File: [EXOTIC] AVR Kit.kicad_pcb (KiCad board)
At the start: 2 copper layers, 100 x 75 mm, 58 parts, among them J1 AVR-ISP-10, J10 5 V Headers, J2 Barrel_Jack_Switch, J3 USB_B, J4 Port A, J5 Port B, J6 Port C + D7, J7 Port D, J9 3.3 V Headers, Q1 AO3401A, SW1 SW_Push, SW2 SW_DPDT_x2, U1 ATmega32A-P, U2 AMS1117-5.0, U3 AMS1117-3.3, U4 LM339, U6 CH340C, Y1 16 MHz

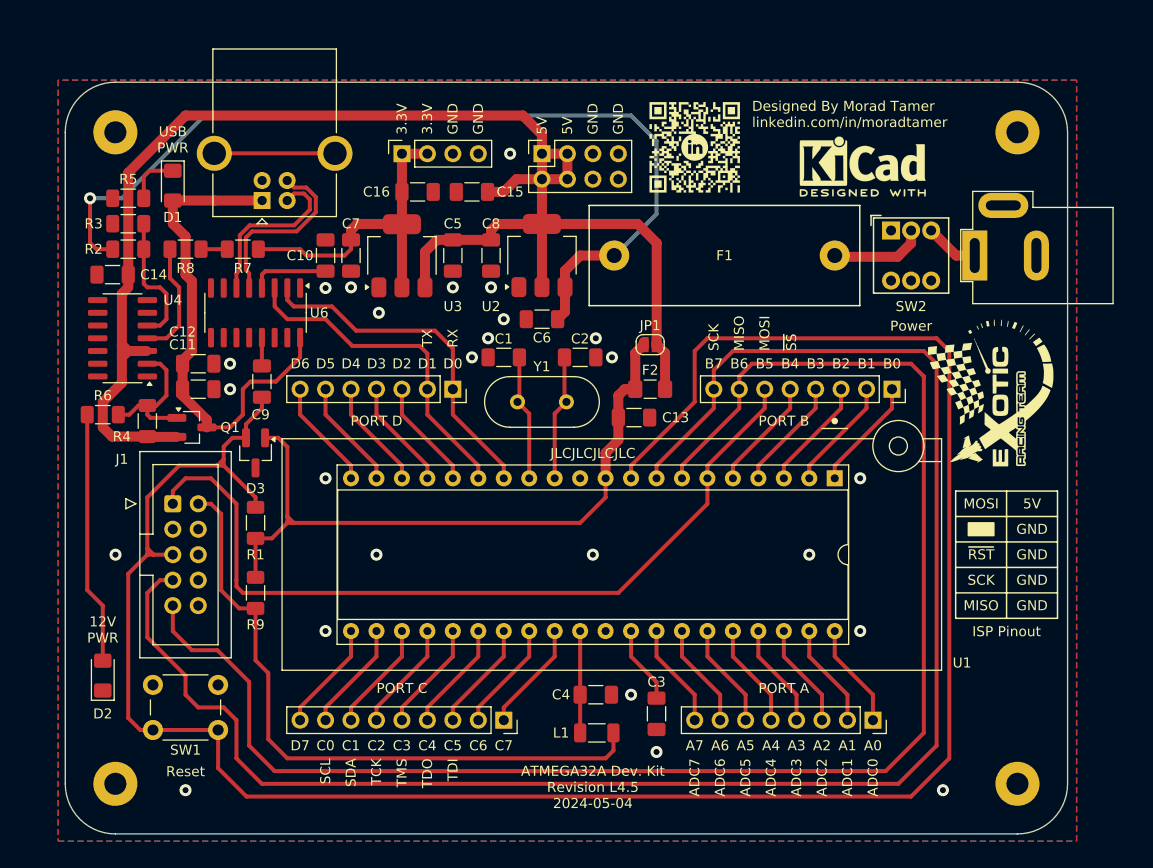
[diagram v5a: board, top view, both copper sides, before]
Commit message: Removed the two LED indicators
Removed the two LED indicators for each power source and replaced them with a single LED for the final 5V rail
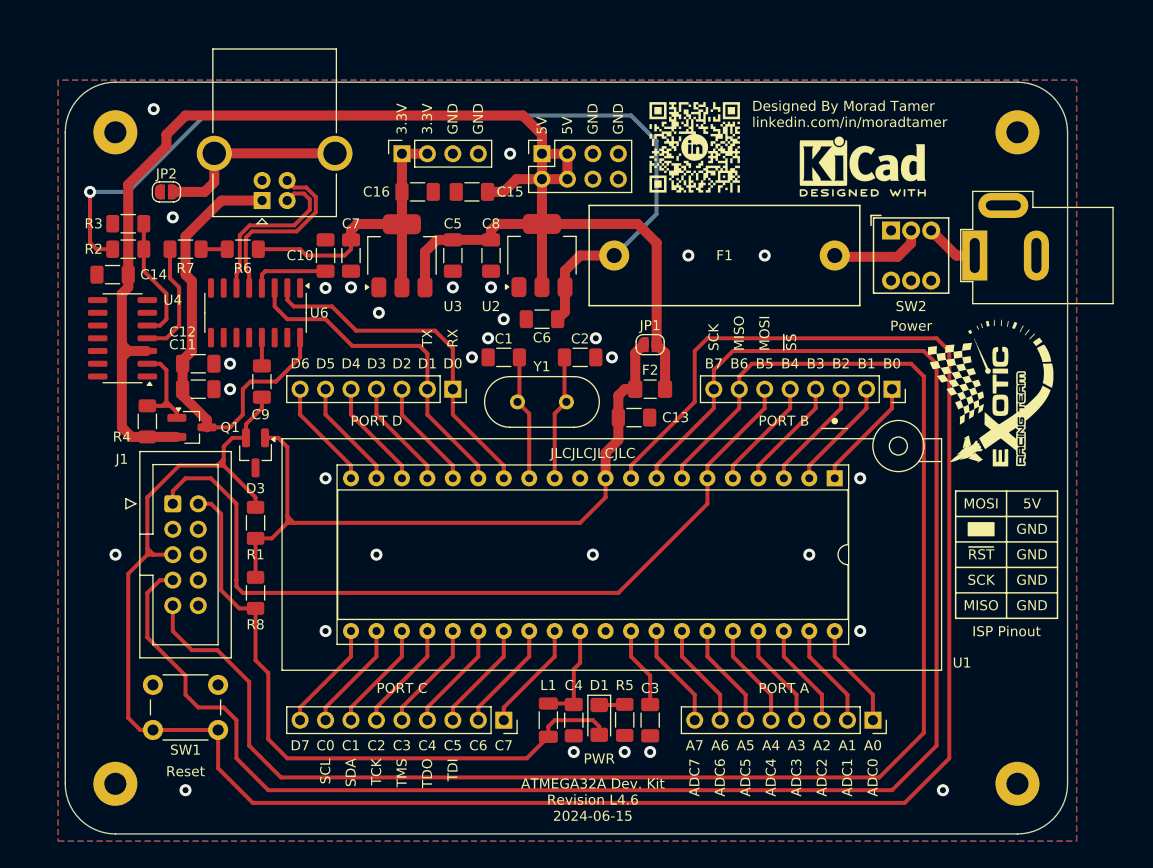
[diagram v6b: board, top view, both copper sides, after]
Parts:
- removed D2: LED, LED_SMD:LED_1206_3216Metric_Pad1.42x1.75mm_HandSolder
- removed the R6 at (118.7, 90.2)
- added JP2: SHLD, Jumper:SolderJumper-2_P1.3mm_Open_RoundedPad1.0x1.5mm, F.Cu at (125.1, 67.9)
- moved R5 71.8 mm to (170.8, 120.6), turned to -90 degrees
- moved D1 68.2 mm to (168.3, 120.6)
- moved L1 5.00 mm to (163.2, 120.7), turned to 90 degrees
- moved C4 3.36 mm to (165.7, 120.7), turned to 90 degrees
- moved C3 0.90 mm to (173.4, 120.7)
- renumbered R7 to R6, R8 to R7, R9 to R8
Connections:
- net /Power Management Circuitry/Comparator renamed Net-(Q1-G)
- D1 pad 2: VBUS -> +5V_{NetTie}
- J3 pad 5: unconnected-(J3-Shield-Pad5) -> Net-(J3-Shield)
- L1 pad 1: Net-(U1-AVCC) -> +5V_{NetTie}
- L1 pad 2: +5V_{NetTie} -> Net-(U1-AVCC)
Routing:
- net Net-(D2-A): track 25.2 -> 0.00 mm
- net Net-(J3-Shield): track 0.00 -> 19.4 mm
- net unconnected-(J3-Shield-Pad5): track 12.0 -> 0.00 mm
- net Net-(Q1-G): track 14.3 -> 10.2 mm
- net VBUS: track 49.4 -> 45.5 mm
- net Net-(D1-K): track 5.31 -> 2.57 mm
- net +5V: track 155.2 -> 152.5 mm
- net Net-(U4A-+): track 13.4 -> 12.6 mm
- net /~{RESET}: track 222.1 -> 222.7 mm
- net /SCK: track 172.0 -> 172.6 mm
- net /MISO: track 156.1 -> 156.6 mm
- net GND: vias 25 -> 30
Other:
- board text added: "PWR"
- board text removed: "12V PWR"
- board text removed: "USB PWR"
